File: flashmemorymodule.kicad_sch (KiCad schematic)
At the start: 2 parts, among them U5 MS5611-01BA

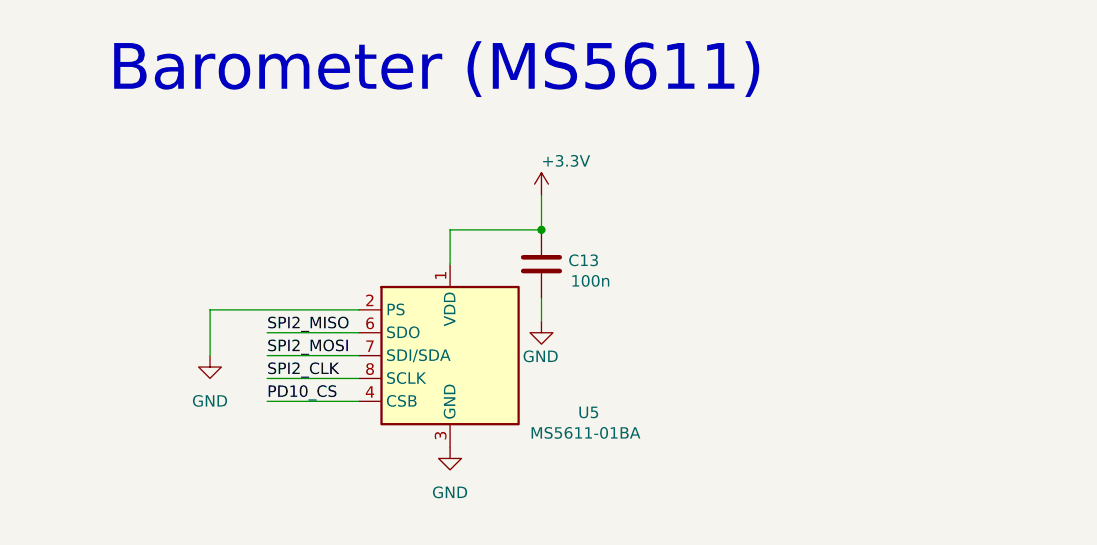
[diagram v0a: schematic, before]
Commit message: Flash memory v2 (#20)
* removed decoupling cap

* fixed missing PE2 pin
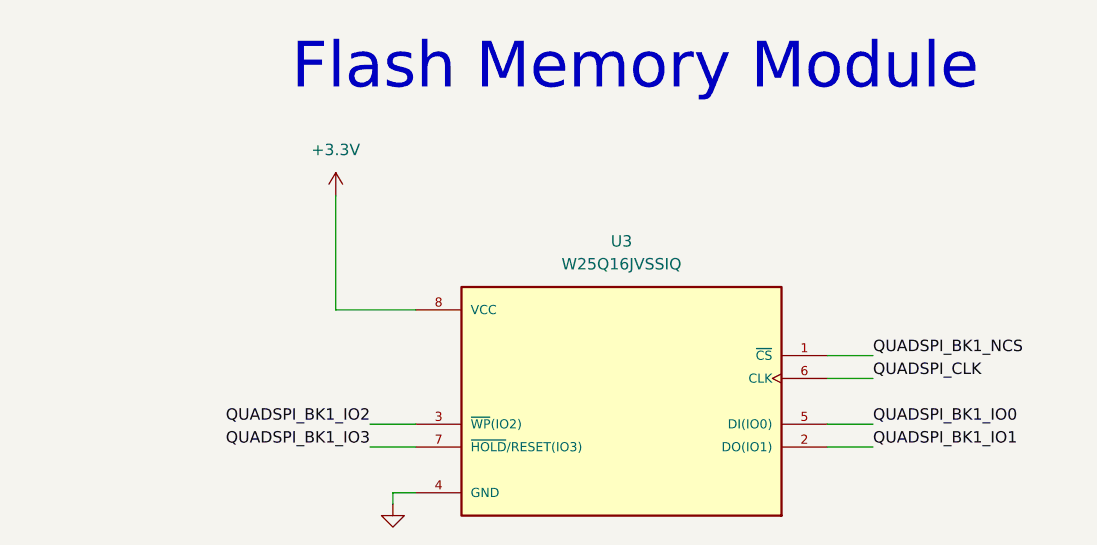
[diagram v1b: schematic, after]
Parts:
- removed C13: 100n, symbol Device:C
- removed U5: MS5611-01BA, Package_LGA:LGA-8_3x5mm_P1.25mm, symbol Sensor_Pressure:MS5611-01BA
- added U3: W25Q16JVSSIQ, W25Q16JVSSIQ:SOIC127P790X216-8N, symbol W25Q16JVSSIQ:W25Q16JVSSIQ
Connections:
- net +3.3V: now also U3.8 (VCC)
- net GND: now also U3.4 (GND)
- new net QUADSPI_BK1_IO0: U3.5 (DI(IO0))
- new net QUADSPI_BK1_IO1: U3.2 (DO(IO1))
- new net QUADSPI_BK1_IO2: U3.3 (~{WP}(IO2))
- new net QUADSPI_BK1_IO3: U3.7 (~{HOLD}/RESET(IO3))
- new net QUADSPI_BK1_NCS: U3.1 (~{CS})
- new net QUADSPI_CLK: U3.6 (CLK)
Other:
- note added: "Flash Memory Module"
- note removed: "Barometer (MS5611)"
